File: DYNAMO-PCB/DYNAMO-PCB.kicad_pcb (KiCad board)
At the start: 2 copper layers, 42 parts, among them J1 HDMI_A, J10 Conn_01x03_Pin, J11 Conn_01x03_Pin, J12 Conn_01x03_Pin, J13 Conn_01x02_Pin, J17 USB3_A, J18 USB3_A, J19 USB3_A, J2 USB3_A, J20 USB3_A, J21 USB3_A, J22 USB3_A, J23 USB3_A, J24 USB3_A, J25 USB3_A, J26 USB_C_Receptacle_USB2.0_16P, J27 USB_C_Receptacle_USB2.0_16P, J28 USB_C_Receptacle_USB2.0_16P, J29 USB_C_Receptacle_USB2.0_16P, J3 Conn_01x03_Pin, J30 USB_C_Receptacle_USB2.0_16P, J31 USB_C_Receptacle_USB2.0_16P, J32 USB3_A, J5 Conn_01x02_Pin, J6 Conn_01x03_Pin, J7 Conn_01x08_Socket, J8 Conn_01x03_Pin, J9 Conn_01x03_Pin, U1 TPS65988DHRSHR, U2 CH7035B-BF, U3 USB7206/KDX

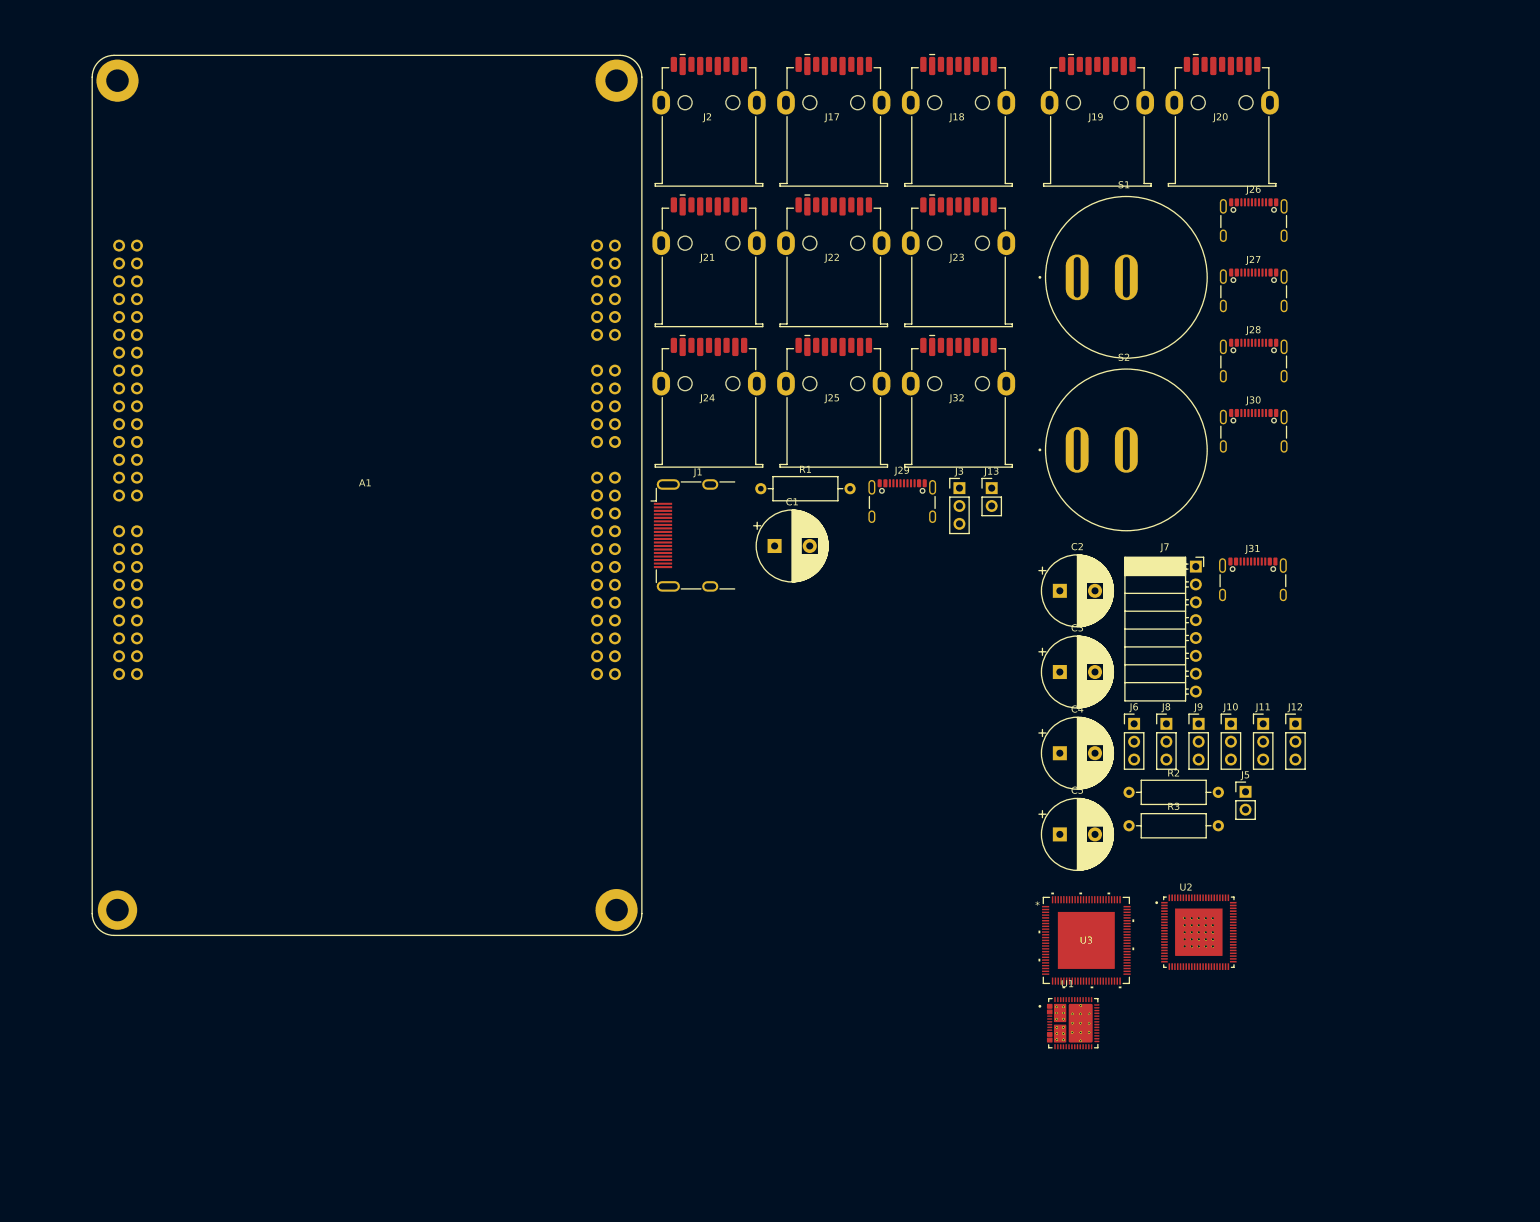
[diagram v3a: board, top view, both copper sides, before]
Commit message: removed unncessary ic
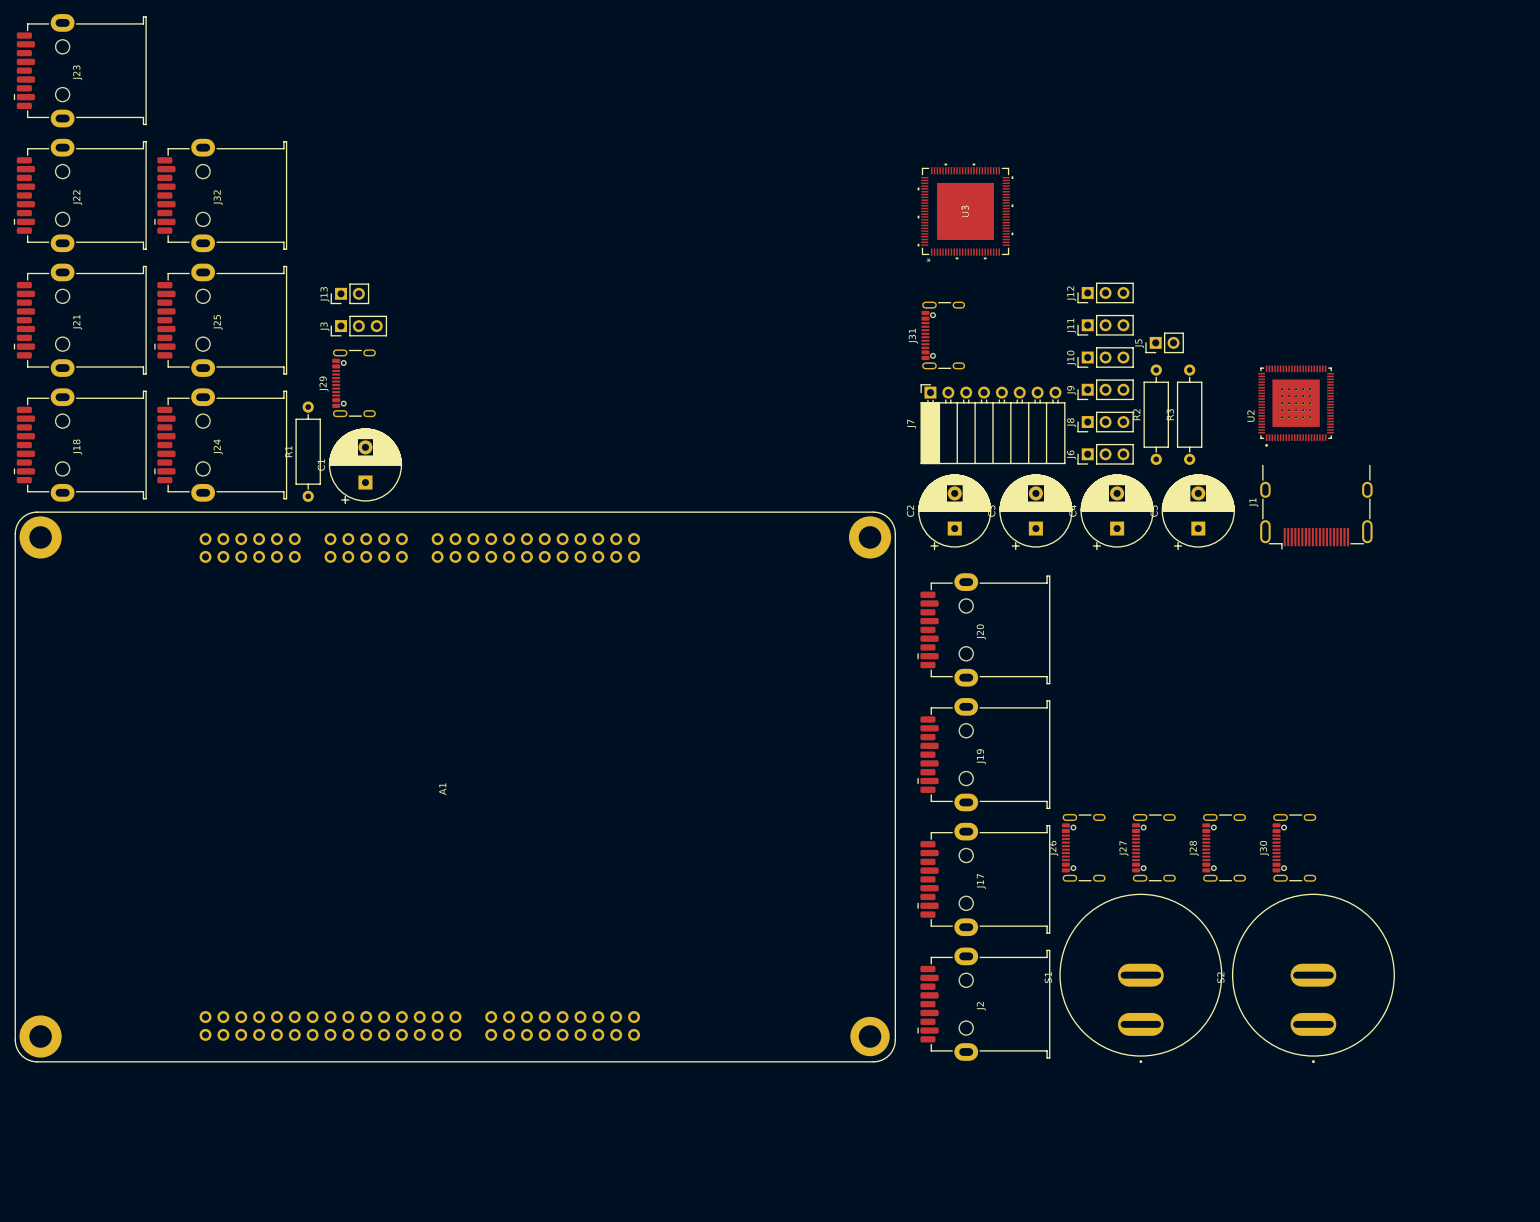
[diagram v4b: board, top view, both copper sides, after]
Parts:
- removed U1: TPS65988DHRSHR, TPS65988DHRSHR:IC_TPS65987DDHRSHR
- moved J18 133.0 mm to (53.9, 75.8), turned to 90 degrees
- moved J2 131.9 mm to (182.5, 155.4), turned to 90 degrees
- moved J23 127.6 mm to (53.9, 22.6), turned to 90 degrees
- moved A1 113.0 mm to (71.7, 159.5), turned to 90 degrees
- moved J17 110.3 mm to (182.5, 137.6), turned to 90 degrees
- moved J32 108.7 mm to (73.9, 40.3), turned to 90 degrees
- moved J22 107.3 mm to (53.9, 40.3), turned to 90 degrees
- moved U3 105.1 mm to (179.8, 42.4), turned to 90 degrees
- moved S1 99.3 mm to (204.7, 151.0), turned to 90 degrees
- moved J13 96.6 mm to (91.0, 54.1), turned to 90 degrees
- moved J19 91.8 mm to (182.5, 119.9), turned to 90 degrees
- moved J26 91.1 mm to (197.8, 132.9), turned to 90 degrees
- moved J3 91.0 mm to (91.0, 58.7), turned to 90 degrees
- moved J1 89.7 mm to (229.7, 85.4), turned to 90 degrees
- moved J21 89.6 mm to (53.9, 58.1), turned to 90 degrees
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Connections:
- J18 pad 1: unconnected-(J18-VBUS-Pad1) -> Net-(J18-VBUS)
- J18 pad 10: unconnected-(J18-SHIELD-Pad10) -> Net-(J18-SHIELD)
- J18 pad 2: unconnected-(J18-D--Pad2) -> Net-(J18-D-)
- J18 pad 3: unconnected-(J18-D+-Pad3) -> Net-(J18-D+)
- J18 pad 4: unconnected-(J18-GND-Pad4) -> Net-(J18-GND)
- J18 pad 5: unconnected-(J18-SSRX--Pad5) -> Net-(J18-SSRX-)
- J18 pad 6: unconnected-(J18-SSRX+-Pad6) -> Net-(J18-SSRX+)
- J18 pad 7: unconnected-(J18-DRAIN-Pad7) -> Net-(J18-DRAIN)
- J18 pad 8: unconnected-(J18-SSTX--Pad8) -> Net-(J18-SSTX-)
- J18 pad 9: unconnected-(J18-SSTX+-Pad9) -> Net-(J18-SSTX+)
- J22 pad 1: unconnected-(J22-VBUS-Pad1) -> Net-(J22-VBUS)
- J22 pad 10: unconnected-(J22-SHIELD-Pad10) -> Net-(J22-SHIELD)
- J22 pad 2: unconnected-(J22-D--Pad2) -> Net-(J22-D-)
- J22 pad 3: unconnected-(J22-D+-Pad3) -> Net-(J22-D+)
- J22 pad 4: unconnected-(J22-GND-Pad4) -> Net-(J22-GND)
- J22 pad 5: unconnected-(J22-SSRX--Pad5) -> Net-(J22-SSRX-)
- J22 pad 6: unconnected-(J22-SSRX+-Pad6) -> Net-(J22-SSRX+)
- J22 pad 7: unconnected-(J22-DRAIN-Pad7) -> Net-(J22-DRAIN)
- J22 pad 8: unconnected-(J22-SSTX--Pad8) -> Net-(J22-SSTX-)
- J22 pad 9: unconnected-(J22-SSTX+-Pad9) -> Net-(J22-SSTX+)
- J23 pad 1: unconnected-(J23-VBUS-Pad1) -> Net-(J18-VBUS)
- J23 pad 10: unconnected-(J23-SHIELD-Pad10) -> Net-(J18-SHIELD)
- J23 pad 2: unconnected-(J23-D--Pad2) -> Net-(J18-D-)
- J23 pad 3: unconnected-(J23-D+-Pad3) -> Net-(J18-D+)
- J23 pad 4: unconnected-(J23-GND-Pad4) -> Net-(J18-GND)
- J23 pad 5: unconnected-(J23-SSRX--Pad5) -> Net-(J18-SSRX-)
- J23 pad 6: unconnected-(J23-SSRX+-Pad6) -> Net-(J18-SSRX+)
- J23 pad 7: unconnected-(J23-DRAIN-Pad7) -> Net-(J18-DRAIN)
- J23 pad 8: unconnected-(J23-SSTX--Pad8) -> Net-(J18-SSTX-)
- J23 pad 9: unconnected-(J23-SSTX+-Pad9) -> Net-(J18-SSTX+)
- J24 pad 1: unconnected-(J24-VBUS-Pad1) -> Net-(J22-VBUS)
- J24 pad 10: unconnected-(J24-SHIELD-Pad10) -> Net-(J22-SHIELD)
- J24 pad 2: unconnected-(J24-D--Pad2) -> Net-(J22-D-)
- J24 pad 3: unconnected-(J24-D+-Pad3) -> Net-(J22-D+)
- J24 pad 4: unconnected-(J24-GND-Pad4) -> Net-(J22-GND)
- J24 pad 5: unconnected-(J24-SSRX--Pad5) -> Net-(J22-SSRX-)
- J24 pad 6: unconnected-(J24-SSRX+-Pad6) -> Net-(J22-SSRX+)
- J24 pad 7: unconnected-(J24-DRAIN-Pad7) -> Net-(J22-DRAIN)
- J24 pad 8: unconnected-(J24-SSTX--Pad8) -> Net-(J22-SSTX-)
- J24 pad 9: unconnected-(J24-SSTX+-Pad9) -> Net-(J22-SSTX+)

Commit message: removed usb7206
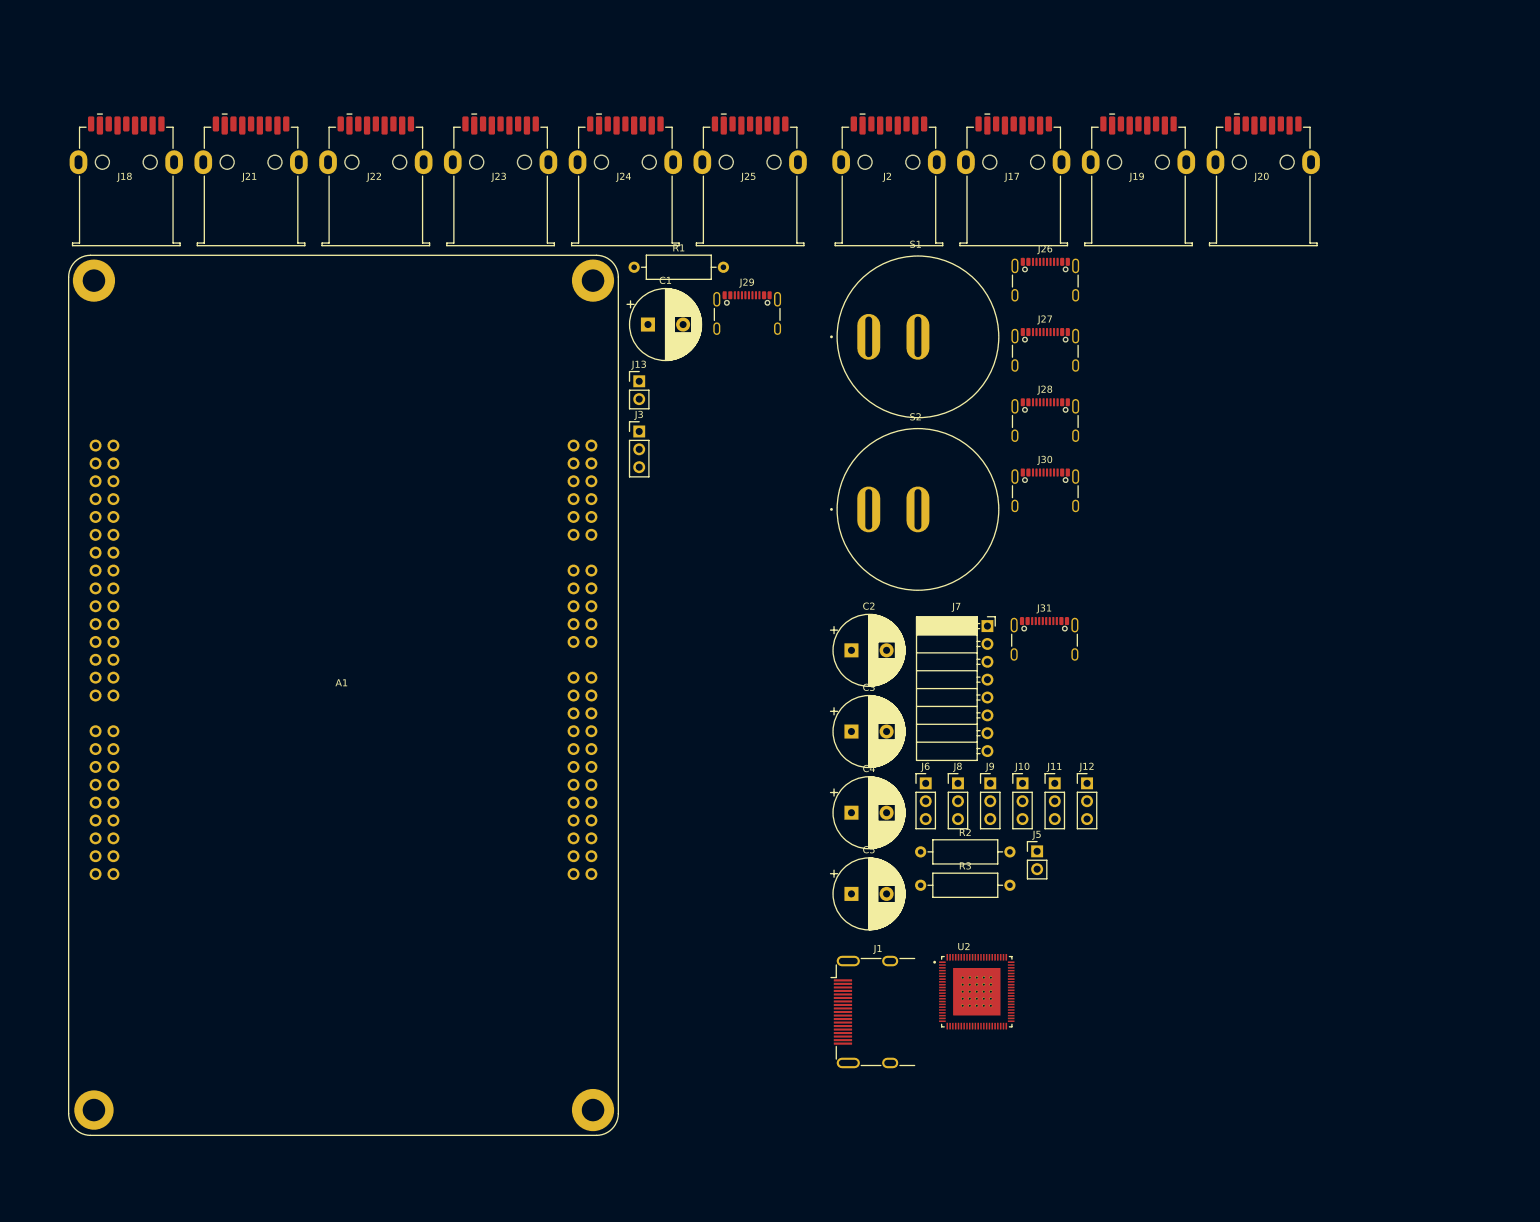
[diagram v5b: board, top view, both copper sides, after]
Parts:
- removed J32: USB3_A, 692122030100:692122030100
- removed U3: USB7206/KDX, ul_USB7206-KDX:VQFN100_KDX_MCH
- moved J2 118.2 mm to (168.7, 37.9), turned to 0 degrees
- moved J17 99.8 mm to (186.5, 37.9), turned to 0 degrees
- moved S1 96.2 mm to (173.0, 60.2), turned to 0 degrees
- moved J1 95.5 mm to (165.7, 156.3), turned to 0 degrees
- moved U2 95.3 mm to (181.4, 153.4), turned to 0 degrees
- moved S2 86.9 mm to (173.0, 84.8), turned to 0 degrees
- moved A1 85.3 mm to (56.0, 75.7), turned to 0 degrees
- moved J19 84.8 mm to (204.2, 37.9), turned to 0 degrees
- moved J26 80.0 mm to (191.2, 53.2), turned to 0 degrees
- moved J25 77.7 mm to (149.0, 37.9), turned to 0 degrees
- moved J20 75.4 mm to (222.0, 37.9), turned to 0 degrees
- moved J5 74.3 mm to (190.0, 133.4), turned to 0 degrees
- moved C5 71.7 mm to (163.6, 139.5), turned to 0 degrees
- moved R3 71.7 mm to (173.4, 138.3), turned to 0 degrees
- moved J27 71.6 mm to (191.2, 63.2), turned to 0 degrees
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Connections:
- J21 pad 1: unconnected-(J21-VBUS-Pad1) -> Net-(J21-VBUS)
- J21 pad 10: unconnected-(J21-SHIELD-Pad10) -> Net-(J21-SHIELD)
- J21 pad 2: unconnected-(J21-D--Pad2) -> Net-(J21-D-)
- J21 pad 3: unconnected-(J21-D+-Pad3) -> Net-(J21-D+)
- J21 pad 4: unconnected-(J21-GND-Pad4) -> Net-(J21-GND)
- J21 pad 5: unconnected-(J21-SSRX--Pad5) -> Net-(J21-SSRX-)
- J21 pad 6: unconnected-(J21-SSRX+-Pad6) -> Net-(J21-SSRX+)
- J21 pad 7: unconnected-(J21-DRAIN-Pad7) -> Net-(J21-DRAIN)
- J21 pad 8: unconnected-(J21-SSTX--Pad8) -> Net-(J21-SSTX-)
- J21 pad 9: unconnected-(J21-SSTX+-Pad9) -> Net-(J21-SSTX+)
- J25 pad 1: unconnected-(J25-VBUS-Pad1) -> Net-(J21-VBUS)
- J25 pad 10: unconnected-(J25-SHIELD-Pad10) -> Net-(J21-SHIELD)
- J25 pad 2: unconnected-(J25-D--Pad2) -> Net-(J21-D-)
- J25 pad 3: unconnected-(J25-D+-Pad3) -> Net-(J21-D+)
- J25 pad 4: unconnected-(J25-GND-Pad4) -> Net-(J21-GND)
- J25 pad 5: unconnected-(J25-SSRX--Pad5) -> Net-(J21-SSRX-)
- J25 pad 6: unconnected-(J25-SSRX+-Pad6) -> Net-(J21-SSRX+)
- J25 pad 7: unconnected-(J25-DRAIN-Pad7) -> Net-(J21-DRAIN)
- J25 pad 8: unconnected-(J25-SSTX--Pad8) -> Net-(J21-SSTX-)
- J25 pad 9: unconnected-(J25-SSTX+-Pad9) -> Net-(J21-SSTX+)
